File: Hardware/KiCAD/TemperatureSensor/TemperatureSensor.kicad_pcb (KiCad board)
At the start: 2 copper layers, 50 parts, among them J1 Conn_01x02, J2 Conn_01x02, J3 Conn_01x02, J4 Conn_01x02, U1 ARDUINO_MICRO_SHIELD, U2 LD1117S33TR_SOT223, U3 MAX31856, U4 MAX31856, U5 MAX31856, U6 MAX31856

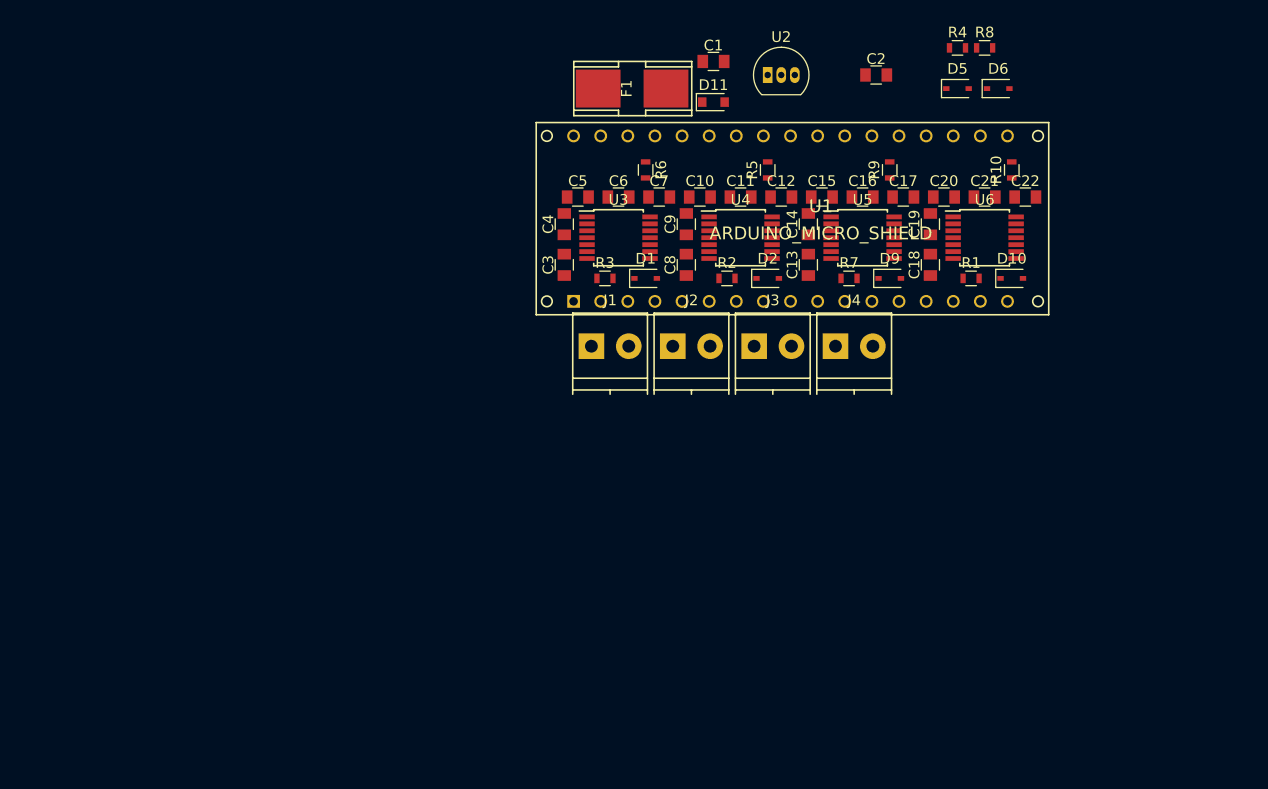
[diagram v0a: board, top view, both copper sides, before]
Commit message: working on temp sensors
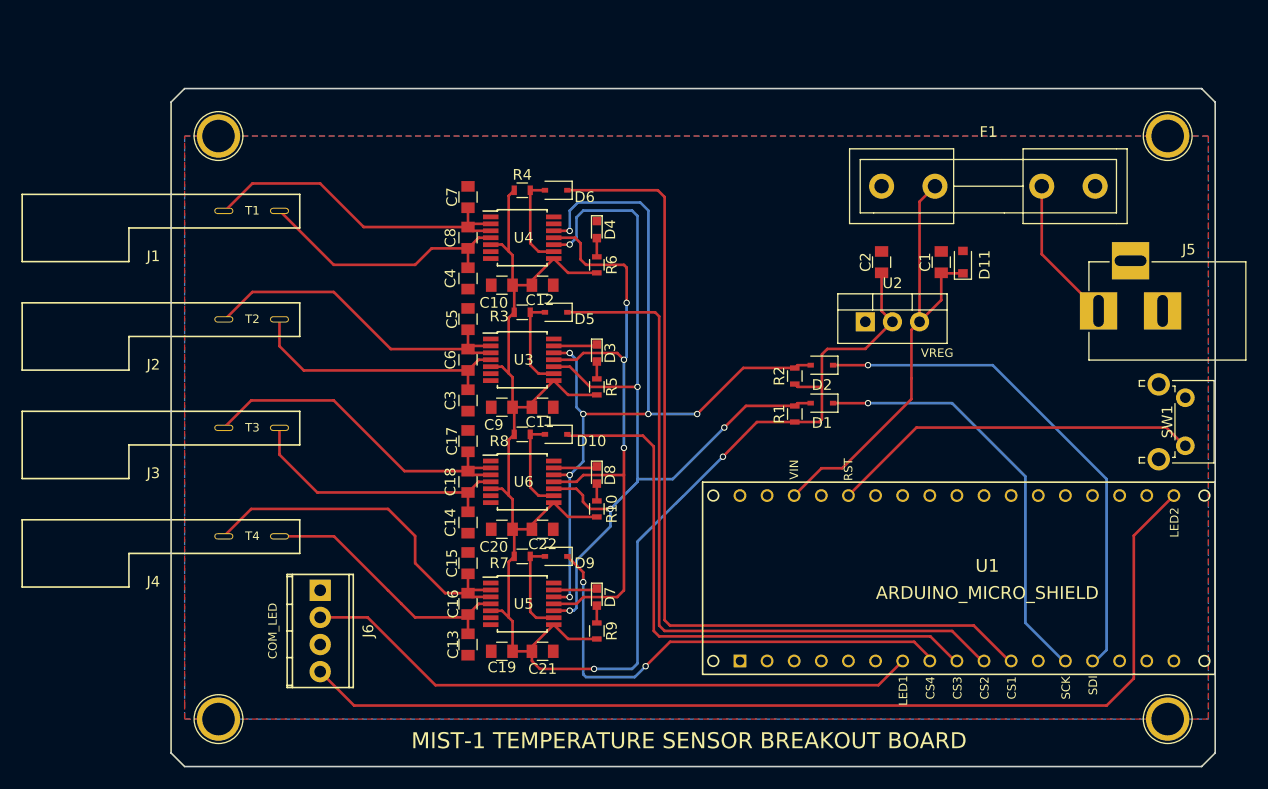
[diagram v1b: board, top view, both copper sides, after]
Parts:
- added ?: 1pin, Connectors:1pin, F.Cu at (207.6, 142.9)
- added ?: 1pin, Connectors:1pin, F.Cu at (118.7, 142.9)
- added ?: 1pin, Connectors:1pin, F.Cu at (118.7, 88.3)
- added ?: 1pin, Connectors:1pin, F.Cu at (207.6, 88.3)
- added D3: LED, LEDs:LED_0603, F.Cu at (154.2, 108.6)
- added D4: LED, LEDs:LED_0603, F.Cu at (154.2, 97.0)
- added D7: LED, LEDs:LED_0603, F.Cu at (154.2, 131.4)
- added D8: LED, LEDs:LED_0603, F.Cu at (154.2, 120.0)
- added J5: Barrel_Jack, Connectors:BARREL_JACK, F.Cu at (201.2, 104.6)
- added J6: Conn_01x04, TerminalBlocks_Phoenix:TerminalBlock_Phoenix_MPT-2.54mm_4pol, F.Cu at (128.3, 130.8)
- added SW1: SW_Push, Buttons_Switches_THT:SW_Tactile_SPST_Angled_PTS645Vx39-2LFS, F.Cu at (209.3, 112.8)
- F1: footprint SMD_Packages:Fuse_SMD -> Fuse_Holders_and_Fuses:Fuseholder5x20_horiz_open_inline_Type-I
- J1, J2, J3, J4: footprint TerminalBlocks_Phoenix:TerminalBlock_Phoenix_PT-3.5mm_2pol -> TemperatureSensor:Thermocouple_Pins
- U2: footprint TO_SOT_Packages_THT:TO-92_Inline_Narrow_Oval -> TO_SOT_Packages_THT:TO-220-3_Vertical
- moved C21 59.4 mm to (149.1, 136.5)
- moved C19 56.7 mm to (145.3, 136.5), turned to 180 degrees
- moved R8 56.4 mm to (147.2, 116.2)
- moved J4 55.0 mm to (124.5, 125.7)
- moved C22 54.9 mm to (149.1, 125.1)
- moved C16 53.1 mm to (142.1, 132.1), turned to 270 degrees
- moved C20 51.8 mm to (145.3, 125.1), turned to 180 degrees
- moved R9 51.2 mm to (154.2, 134.6)
- moved R10 50.2 mm to (154.2, 123.2)
- moved U6 49.0 mm to (147.2, 120.7)
- moved C18 47.8 mm to (142.1, 120.7), turned to 270 degrees
- moved C13 47.8 mm to (142.1, 135.9), turned to 270 degrees
- moved C15 47.7 mm to (142.1, 128.3), turned to 90 degrees
- moved U5 46.8 mm to (147.2, 132.1)
- moved C17 46.7 mm to (142.1, 116.8), turned to 90 degrees
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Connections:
- C1 pad 1: Net-(C1-Pad1) -> VIN
- D11 pad 1: Net-(C1-Pad1) -> VIN
- F1 pad 1: Net-(C1-Pad1) -> VIN
- F1 pad 2: +5V -> Net-(F1-Pad2)
- U1 pad 10: Net-(U1-Pad10) -> (no net)
- U1 pad 11: Net-(U1-Pad11) -> (no net)
- U1 pad 12: Net-(U1-Pad12) -> (no net)
- U1 pad 13: Net-(U1-Pad13) -> COM_LED2
- U1 pad 2: Net-(U1-Pad2) -> COM_LED1
- U1 pad 3: CS1 -> CS4
- U1 pad 3.3V: Net-(U1-Pad3.3V) -> (no net)
- U1 pad 4: CS2 -> CS3
- U1 pad 5: CS3 -> CS2
- U1 pad 5V: +5V -> (no net)
- U1 pad 6: CS4 -> CS1
- U1 pad 7: Net-(U1-Pad7) -> SDO
- U1 pad 8: Net-(U1-Pad8) -> SCK
- U1 pad 9: Net-(U1-Pad9) -> SDI
- U1 pad A0: Net-(U1-PadA0) -> (no net)
- U1 pad A1: Net-(U1-PadA1) -> (no net)
- U1 pad A2: Net-(U1-PadA2) -> (no net)
- U1 pad A3: Net-(U1-PadA3) -> (no net)
- U1 pad A4: Net-(U1-PadA4) -> (no net)
- U1 pad A5: Net-(U1-PadA5) -> (no net)
- U1 pad AREF: Net-(U1-PadAREF) -> (no net)
- U1 pad MI: SDI -> (no net)
- U1 pad MO: SDO -> (no net)
- U1 pad RX: Net-(U1-PadRX) -> (no net)
- U1 pad SCK: SCK -> (no net)
- U1 pad SS: Net-(U1-PadSS) -> (no net)
- U1 pad TX: Net-(U1-PadTX) -> (no net)
- U1 pad VI: Net-(U1-PadVI) -> VIN
- U2 pad 3: Net-(C1-Pad1) -> VIN
- U3 pad 6: Net-(U3-Pad6) -> (no net)
- U3 pad 7: Net-(U3-Pad7) -> (no net)
- U4 pad 6: Net-(U4-Pad6) -> (no net)
- U4 pad 7: Net-(U4-Pad7) -> (no net)
- U5 pad 6: Net-(U5-Pad6) -> (no net)
- U5 pad 7: Net-(U5-Pad7) -> (no net)
- U6 pad 6: Net-(U6-Pad6) -> (no net)
- U6 pad 7: Net-(U6-Pad7) -> (no net)
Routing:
- net +3V3: track 0.00 -> 158.8 mm, vias 0 -> 2
- net COM_LED2: track 0.00 -> 97.2 mm
- net SCK_3V3: track 0.00 -> 86.1 mm, vias 0 -> 5
- net CS1: track 0.00 -> 83.0 mm
- net SDI_3V3: track 0.00 -> 82.1 mm, vias 0 -> 7
- net CS2: track 0.00 -> 69.5 mm
- net SDO: track 0.00 -> 60.3 mm, vias 0 -> 3
- net COM_LED1: track 0.00 -> 58.1 mm
- net CS3: track 0.00 -> 55.7 mm
- net SDI: track 0.00 -> 47.8 mm, vias 0 -> 1
- net CS4: track 0.00 -> 46.5 mm, vias 0 -> 2
- net VIN: track 0.00 -> 43.1 mm
- net SCK: track 0.00 -> 39.8 mm, vias 0 -> 1
- net Net-(SW1-Pad2): track 0.00 -> 35.4 mm
- net T4-: track 0.00 -> 35.2 mm
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- added copper zone on B.Cu, net GND
- added copper zone on F.Cu, net GND
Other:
- board outline added: 97.8 x 63.5 mm
- board text added: "COM_LED"
- board text added: "CS1"
- board text added: "CS2"
- board text added: "CS3"
- board text added: "CS4"
- board text added: "LED1"
- board text added: "LED2"
- board text added: "MIST-1 TEMPERATURE SENSOR BREAKOUT BOARD"
- board text added: "RST"
- board text added: "SCK"
- board text added: "SDI"
- board text added: "T1"
- board text added: "T2"
- board text added: "T3"
- board text added: "T4"
- board text added: "VIN"
- board text added: "VREG"
